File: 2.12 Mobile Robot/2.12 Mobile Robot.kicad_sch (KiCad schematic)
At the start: 27 parts, among them J1 Motor Control R, J2 Motor Control L, J3 GND, J4 Motor Power R, J5 Battery Power, J6 Motor Power L, J7 3.3V, J8 UART, J9 5V, SW1 SW_PWR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

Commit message: Fully routed
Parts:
- R3: renamed from RSE1; Name (none) -> RSE1
- R4: renamed from RCs1; Name (none) -> RCs1
- renumbered R_MTR1 to R1, R_MTR2 to R2, R_MOTOR1 to R5
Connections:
- net L_MOTOR: now reaches F2.2, J6.2
- net R_MOTOR: now reaches F1.2, J4.2
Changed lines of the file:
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@@
   (junction (at 213.36 119.38) (diameter 0) (color 0 0 0 0)
   )
+  (junction (at 206.375 85.09) (diameter 0) (color 0 0 0 0)
+  )
   (junction (at 252.73 119.38) (diameter 0) (color 0 0 0 0)
   )
@@
   (junction (at 201.295 121.285) (diameter 0) (color 0 0 0 0)
   )
+  (junction (at 208.915 64.135) (diameter 0) (color 0 0 0 0)
+  )
   (junction (at 252.73 118.11) (diameter 0) (color 0 0 0 0)
   )
@@
   (junction (at 201.295 116.205) (diameter 0) (color 0 0 0 0)
   )
-  (wire (pts (xy 205.105 64.135) (xy 211.455 64.135))
+  (wire (pts (xy 205.105 64.135) (xy 208.915 64.135))
     (stroke (width 0) (type default))
   )
@@
     (stroke (width 0) (type default))
   )
+  (wire (pts (xy 208.915 69.85) (xy 208.915 64.135))
+    (stroke (width 0) (type default))
+  )
   (wire (pts (xy 233.68 34.925) (xy 244.475 34.925))
     (stroke (width 0) (type default))
@@
     (stroke (width 0) (type default))
   )
+  (wire (pts (xy 206.375 92.075) (xy 206.375 85.09))
+    (stroke (width 0) (type default))
+  )
   (wire (pts (xy 198.755 142.24) (xy 201.295 142.24))
     (stroke (width 0) (type default))
@@
     (stroke (width 0) (type default))
   )
+  (wire (pts (xy 209.55 92.075) (xy 206.375 92.075))
+    (stroke (width 0) (type default))
+  )
   (wire (pts (xy 201.295 113.665) (xy 201.295 116.205))
     (stroke (width 0) (type default))
@@
     (stroke (width 0) (type default))
   )
-  (wire (pts (xy 204.47 85.09) (xy 208.28 85.09))
+  (wire (pts (xy 204.47 85.09) (xy 206.375 85.09))
     (stroke (width 0) (type default))
   )
@@
     (stroke (width 0) (type default))
   )
+  (wire (pts (xy 209.55 69.85) (xy 208.915 69.85))
+    (stroke (width 0) (type default))
+  )
   (wire (pts (xy 73.025 43.18) (xy 83.82 43.18))
     (stroke (width 0) (type default))
   )
+  (wire (pts (xy 206.375 85.09) (xy 208.28 85.09))
+    (stroke (width 0) (type default))
+  )
+  (wire (pts (xy 133.985 71.755) (xy 138.43 71.755))
+    (stroke (width 0) (type default))
+  )
   (wire (pts (xy 204.47 76.2) (xy 204.47 80.01))
     (stroke (width 0) (type default))
@@
   )
   (wire (pts (xy 213.36 119.38) (xy 213.36 121.92))
+    (stroke (width 0) (type default))
+  )
+  (wire (pts (xy 208.915 64.135) (xy 211.455 64.135))
     (stroke (width 0) (type default))
   )
@@
     (effects (font (size 1.27 1.27)) (justify right bottom))
   )
+  (label "L_MOTOR" (at 209.55 69.85 0) (fields_autoplaced)
+    (effects (font (size 1.27 1.27)) (justify left bottom))
+  )
   (label "VBAT_IN" (at 207.645 45.085 0) (fields_autoplaced)
     (effects (font (size 1.27 1.27)) (justify left bottom))
@@
     (effects (font (size 1.27 1.27)) (justify left bottom))
   )
+  (label "R_MOTOR" (at 209.55 92.075 0) (fields_autoplaced)
+    (effects (font (size 1.27 1.27)) (justify left bottom))
+  )
   (label "VBAT_MOTOR" (at 78.74 168.91 0) (fields_autoplaced)
     (effects (font (size 1.27 1.27)) (justify left bottom))
+  )
+  (label "VBAT" (at 133.985 71.755 180) (fields_autoplaced)
+    (effects (font (size 1.27 1.27)) (justify right bottom))
   )
   (label "DIR2_R" (at 73.025 50.8 0) (fields_autoplaced)
@@
   (symbol (lib_id "Device:R_US") (at 153.035 170.18 0) (unit 1)
     (in_bom yes) (on_board yes) (dnp no)
-    (property "Reference" "R_MOTOR1" (at 160.02 172.085 0)
+    (property "Reference" "R5" (at 160.02 172.085 0)
       (effects (font (size 1.27 1.27)))
     )
@@
       (project "2.12 Mobile Robot"
         (path "/7775d959-b998-472b-ab8b-c8b5c0f34c21"
-          (reference "R_MOTOR1") (unit 1)
+          (reference "R5") (unit 1)
         )
       )
@@
   (symbol (lib_id "Device:R_Small_US") (at 27.94 170.815 0) (unit 1)
     (in_bom yes) (on_board yes) (dnp no)
-    (property "Reference" "R_MTR1" (at 30.48 168.91 0)
+    (property "Reference" "R1" (at 30.48 168.91 0)
       (effects (font (size 1.27 1.27)) (justify left))
     )
@@
       (project "2.12 Mobile Robot"
         (path "/7775d959-b998-472b-ab8b-c8b5c0f34c21"
-          (reference "R_MTR1") (unit 1)
+          (reference "R1") (unit 1)
         )
       )
@@
   (symbol (lib_id "Device:R_Small_US") (at 40.005 177.8 0) (mirror y) (unit 1)
     (in_bom yes) (on_board yes) (dnp no)
-    (property "Reference" "RSE1" (at 37.465 177.165 0)
+    (property "Reference" "R3" (at 37.465 177.165 0)
       (effects (font (size 1.27 1.27)) (justify left))
     )
@@
       (effects (font (size 1.27 1.27)) hide)
     )
-    (pin "1")
-    (pin "2")
-    (instances
-      (project "2.12 Mobile Robot"
-        (path "/7775d959-b998-472b-ab8b-c8b5c0f34c21"
-          (reference "RSE1") (unit 1)
+    (property "Name" "RSE1" (at 40.005 177.8 0)
+      (effects (font (size 1.27 1.27)) hide)
+    )
+    (pin "1")
+    (pin "2")
+    (instances
+      (project "2.12 Mobile Robot"
+        (path "/7775d959-b998-472b-ab8b-c8b5c0f34c21"
+          (reference "R3") (unit 1)
         )
       )
@@
   (symbol (lib_id "Device:R_Small_US") (at 75.565 177.8 0) (unit 1)
     (in_bom yes) (on_board yes) (dnp no) (fields_autoplaced)
-    (property "Reference" "RCs1" (at 78.105 177.165 0)
+    (property "Reference" "R4" (at 78.105 177.165 0)
       (effects (font (size 1.27 1.27)) (justify left))
     )
@@
       (effects (font (size 1.27 1.27)) hide)
     )
-    (pin "1")
-    (pin "2")
-    (instances
-      (project "2.12 Mobile Robot"
-        (path "/7775d959-b998-472b-ab8b-c8b5c0f34c21"
-          (reference "RCs1") (unit 1)
+    (property "Name" "RCs1" (at 75.565 177.8 0)
+      (effects (font (size 1.27 1.27)) hide)
+    )
+    (pin "1")
+    (pin "2")
+    (instances
+      (project "2.12 Mobile Robot"
+        (path "/7775d959-b998-472b-ab8b-c8b5c0f34c21"
+          (reference "R4") (unit 1)
         )
       )
@@
   (symbol (lib_id "power:PWR_FLAG") (at 217.805 40.005 0) (unit 1)
     (in_bom yes) (on_board yes) (dnp no)
-    (property "Reference" "#FLG05" (at 217.805 38.1 0)
+    (property "Reference" "#FLG04" (at 217.805 38.1 0)
       (effects (font (size 1.27 1.27)) hide)
     )
@@
       (project "2.12 Mobile Robot"
         (path "/7775d959-b998-472b-ab8b-c8b5c0f34c21"
-          (reference "#FLG05") (unit 1)
+          (reference "#FLG04") (unit 1)
         )
       )
@@
   (symbol (lib_id "Device:R_Small_US") (at 27.94 175.895 0) (mirror y) (unit 1)
     (in_bom yes) (on_board yes) (dnp no)
-    (property "Reference" "R_MTR2" (at 26.67 175.26 0)
+    (property "Reference" "R2" (at 26.67 175.26 0)
       (effects (font (size 1.27 1.27)) (justify left))
     )
@@
       (project "2.12 Mobile Robot"
         (path "/7775d959-b998-472b-ab8b-c8b5c0f34c21"
-          (reference "R_MTR2") (unit 1)
-        )
-      )
+          (reference "R2") (unit 1)
+        )
+      )

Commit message: Made footprints from project libraries
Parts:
- A1: footprint Adafruit:Adafruit_BNO085 -> 2.12_Mobile_Robot:Adafruit_BNO085
- U1: footprint 2.004:DPAK85P972X240-8N -> 2.12_Mobile_Robot:DPAK85P972X240-8N
- U2: footprint footprints:ProS3_TH -> 2.12_Mobile_Robot:ProS3_TH
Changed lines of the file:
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@@
       (effects (font (size 1.27 1.27)))
     )
-    (property "Footprint" "Adafruit:Adafruit_BNO085" (at 38.735 104.14 0)
+    (property "Footprint" "2.12_Mobile_Robot:Adafruit_BNO085" (at 38.735 104.14 0)
       (effects (font (size 1.27 1.27)) hide)
     )
@@
       (effects (font (size 1.27 1.27)))
     )
-    (property "Footprint" "footprints:ProS3_TH" (at 58.547 49.022 0)
+    (property "Footprint" "2.12_Mobile_Robot:ProS3_TH" (at 58.547 49.022 0)
       (effects (font (size 1.27 1.27)) hide)
     )
@@
       (effects (font (size 1.27 1.27)))
     )
-    (property "Footprint" "2.004:DPAK85P972X240-8N" (at 57.785 209.55 0)
+    (property "Footprint" "2.12_Mobile_Robot:DPAK85P972X240-8N" (at 57.785 209.55 0)
       (effects (font (size 1.27 1.27)) (justify bottom) hide)
     )

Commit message: Finesse
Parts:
- A1: footprint 2.12_Mobile_Robot:Adafruit_BNO085 -> Adafruit:Adafruit_BNO085
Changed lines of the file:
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@@
       (effects (font (size 1.27 1.27)))
     )
-    (property "Footprint" "2.12_Mobile_Robot:Adafruit_BNO085" (at 38.735 104.14 0)
+    (property "Footprint" "Adafruit:Adafruit_BNO085" (at 38.735 104.14 0)
       (effects (font (size 1.27 1.27)) hide)
     )

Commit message: Added silkscreen callouts and fixed resistors
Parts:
- R1, R2, R3, R4, R5: footprint Resistor_SMD:R_0201_0603Metric_Pad0.64x0.40mm_HandSolder -> Resistor_SMD:R_0603_1608Metric
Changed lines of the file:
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@@
       (effects (font (size 1.27 1.27)))
     )
-    (property "Footprint" "Resistor_SMD:R_0201_0603Metric_Pad0.64x0.40mm_HandSolder" (at 154.051 170.434 90)
+    (property "Footprint" "Resistor_SMD:R_0603_1608Metric" (at 154.051 170.434 90)
       (effects (font (size 1.27 1.27)) hide)
     )
@@
       (effects (font (size 1.27 1.27)) (justify left))
     )
-    (property "Footprint" "Resistor_SMD:R_0201_0603Metric_Pad0.64x0.40mm_HandSolder" (at 27.94 170.815 0)
+    (property "Footprint" "Resistor_SMD:R_0603_1608Metric" (at 27.94 170.815 0)
       (effects (font (size 1.27 1.27)) hide)
     )
@@
       (effects (font (size 1.27 1.27)) (justify left))
     )
-    (property "Footprint" "Resistor_SMD:R_0201_0603Metric_Pad0.64x0.40mm_HandSolder" (at 40.005 177.8 0)
+    (property "Footprint" "Resistor_SMD:R_0603_1608Metric" (at 40.005 177.8 0)
       (effects (font (size 1.27 1.27)) hide)
     )
@@
       (effects (font (size 1.27 1.27)) (justify left))
     )
-    (property "Footprint" "Resistor_SMD:R_0201_0603Metric_Pad0.64x0.40mm_HandSolder" (at 75.565 177.8 0)
+    (property "Footprint" "Resistor_SMD:R_0603_1608Metric" (at 75.565 177.8 0)
       (effects (font (size 1.27 1.27)) hide)
     )
@@
       (effects (font (size 1.27 1.27)) (justify left))
     )
-    (property "Footprint" "Resistor_SMD:R_0201_0603Metric_Pad0.64x0.40mm_HandSolder" (at 27.94 175.895 0)
-      (effects (font (size 1.27 1.27)) hide)
-    )
+    (property "Footprint" "Resistor_SMD:R_0603_1608Metric" (at 27.94 175.895 0)
+      (effects (font (size 1.27 1.27)) hide)
+    )

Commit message: About to add JLCPCB libraries
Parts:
- removed E1: FL Encoder, Connector_JST:JST_PH_S4B-PH-SM4-TB_1x04-1MP_P2.00mm_Horizontal, symbol Connector:Encoder
- removed E2: BL Encoder, Connector_JST:JST_PH_S4B-PH-SM4-TB_1x04-1MP_P2.00mm_Horizontal, symbol Connector:Encoder
- removed E3: FR Encoder, Connector_JST:JST_PH_S4B-PH-SM4-TB_1x04-1MP_P2.00mm_Horizontal, symbol Connector:Encoder
- removed E4: BR Encoder, Connector_JST:JST_PH_S4B-PH-SM4-TB_1x04-1MP_P2.00mm_Horizontal, symbol Connector:Encoder
- added J10: FL Encoder, Connector_JST:JST_PH_S4B-PH-SM4-TB_1x04-1MP_P2.00mm_Horizontal, symbol Connector_Generic_MountingPin:Conn_01x04_MountingPin
- added J11: BL Encoder, Connector_JST:JST_PH_S4B-PH-SM4-TB_1x04-1MP_P2.00mm_Horizontal, symbol Connector_Generic_MountingPin:Conn_01x04_MountingPin
- added J12: FR Encoder, Connector_JST:JST_PH_S4B-PH-SM4-TB_1x04-1MP_P2.00mm_Horizontal, symbol Connector_Generic_MountingPin:Conn_01x04_MountingPin
- added J13: BR Encoder, Connector_JST:JST_PH_S4B-PH-SM4-TB_1x04-1MP_P2.00mm_Horizontal, symbol Connector_Generic_MountingPin:Conn_01x04_MountingPin
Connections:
- net +3.3V: now also J10.3 (Pin_3), J11.3 (Pin_3), J12.3 (Pin_3), J13.3 (Pin_3)
- net GND: now also J10.4 (Pin_4), J10.MP (MountPin), J11.4 (Pin_4), J11.MP (MountPin), J12.4 (Pin_4), J12.MP (MountPin), J13.4 (Pin_4), J13.MP (MountPin)
- net HALL_BL_A: now also J11.1 (Pin_1)
- net HALL_BL_B: now also J11.2 (Pin_2)
- net HALL_BR_A: now also J13.1 (Pin_1)
- net HALL_BR_B: now also J13.2 (Pin_2)
- net HALL_FL_A: now also J10.1 (Pin_1)
- net HALL_FL_B: now also J10.2 (Pin_2)
- net HALL_FR_A: now also J12.1 (Pin_1)
- net HALL_FR_B: now also J12.2 (Pin_2)

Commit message: Tentatively ready for production
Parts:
- A1, U2: now left out of the parts list
- D1: footprint LED_SMD:LED_0603_1608Metric -> footprint:LED0603; symbol Device:LED -> jlcpcb-diodes:0603,Red; LCSC (none) -> C2286; MPN C434423 -> (none)
- J4, J6: LCSC (none) -> C2913282
- J5: footprint Connector_AMASS:AMASS_XT60PW-M_1x02_P7.20mm_Horizontal -> Connector_AMASS:AMASS_XT30PW-M_1x02_P2.50mm_Horizontal; LCSC (none) -> C2913282
- J9, SW1: now in the parts list
- R1, R2: footprint Resistor_SMD:R_0603_1608Metric -> footprint:0603_1608Metric; symbol Device:R_Small_US -> jlcpcb-basic-resistor:0603,15k; LCSC (none) -> C22809; MFG (none) -> UNI-ROYAL(Uniroyal Elec); MFGPN (none) -> 0603WAF1502T5E; MPN C114661 -> (none)
- R3: footprint Resistor_SMD:R_0603_1608Metric -> footprint:0603_1608Metric; symbol Device:R_Small_US -> jlcpcb-basic-resistor:0603,15k; LCSC (none) -> C22809; MFG (none) -> UNI-ROYAL(Uniroyal Elec); MFGPN (none) -> 0603WAF1502T5E; MPN C114661 -> (none); Name RSE1 -> (none)
- R4: footprint Resistor_SMD:R_0603_1608Metric -> footprint:0603_1608Metric; symbol Device:R_Small_US -> jlcpcb-basic-resistor:0603,15k; LCSC (none) -> C22809; MFG (none) -> UNI-ROYAL(Uniroyal Elec); MFGPN (none) -> 0603WAF1502T5E; MPN C114661 -> (none); Name RCs1 -> (none)
- R5: footprint Resistor_SMD:R_0603_1608Metric -> footprint:0603_1608Metric; symbol Device:R_US -> jlcpcb-basic-resistor:0603,1k; LCSC (none) -> C21190; MFG (none) -> UNI-ROYAL(Uniroyal Elec); MFGPN (none) -> 0603WAF1001T5E
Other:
- sheet Buck ports: added none; removed VBAT_MCU

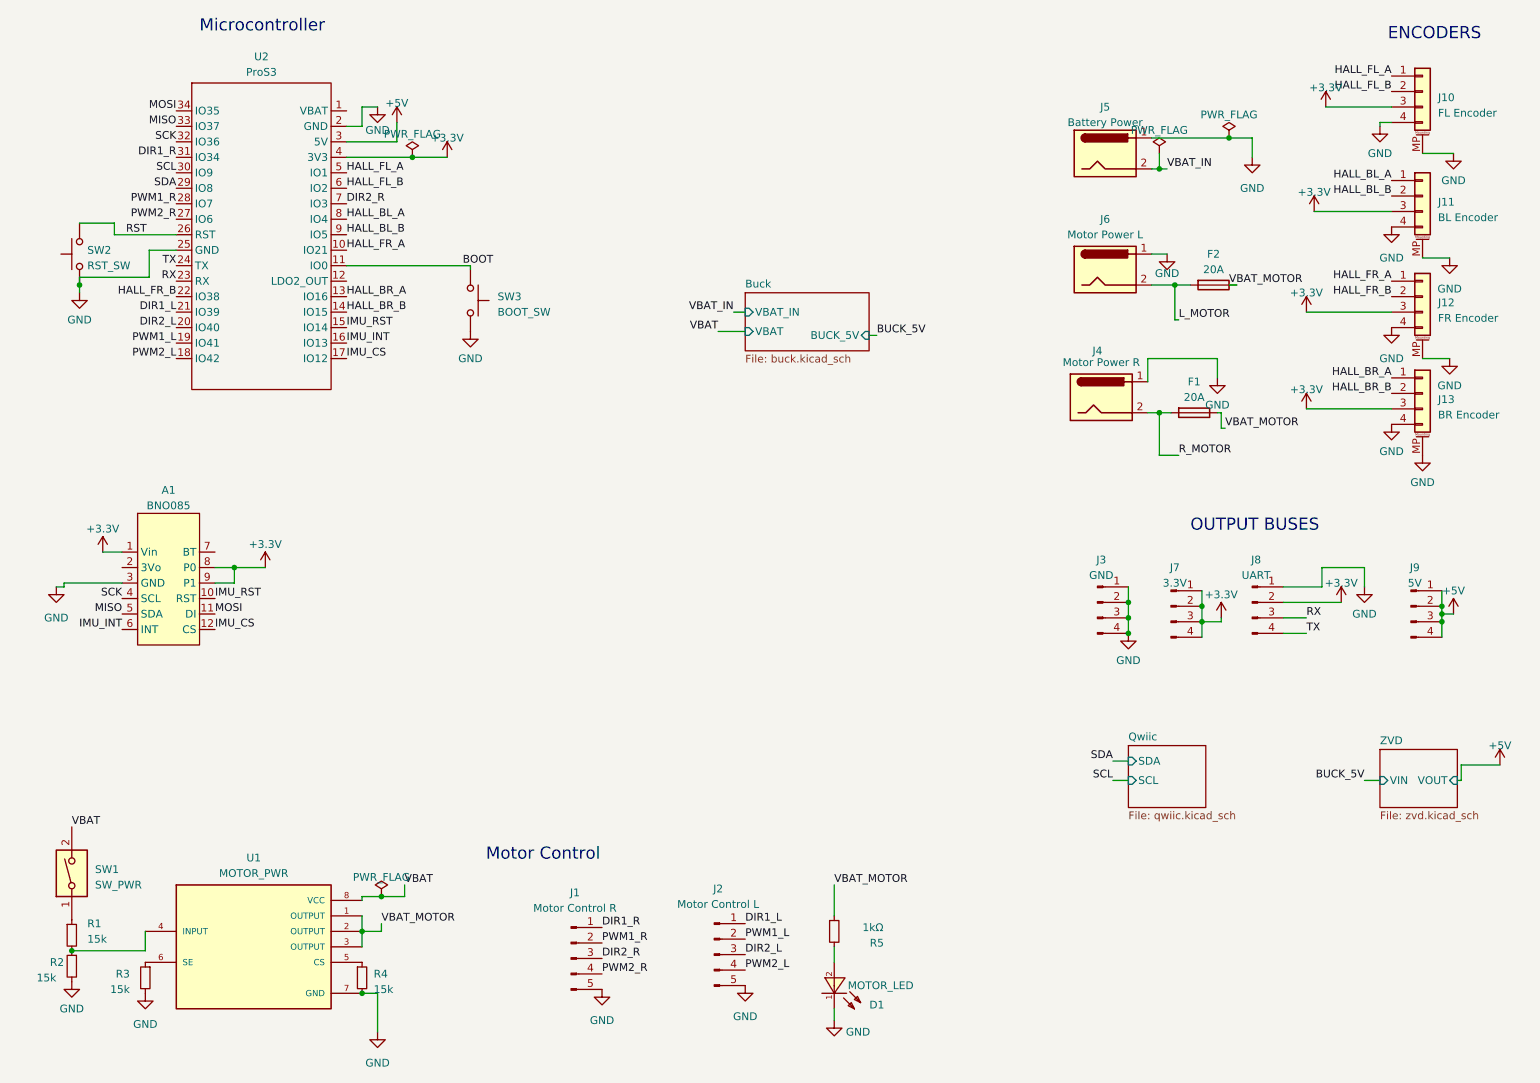
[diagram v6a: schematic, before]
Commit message: Updated silkscreen to be generic
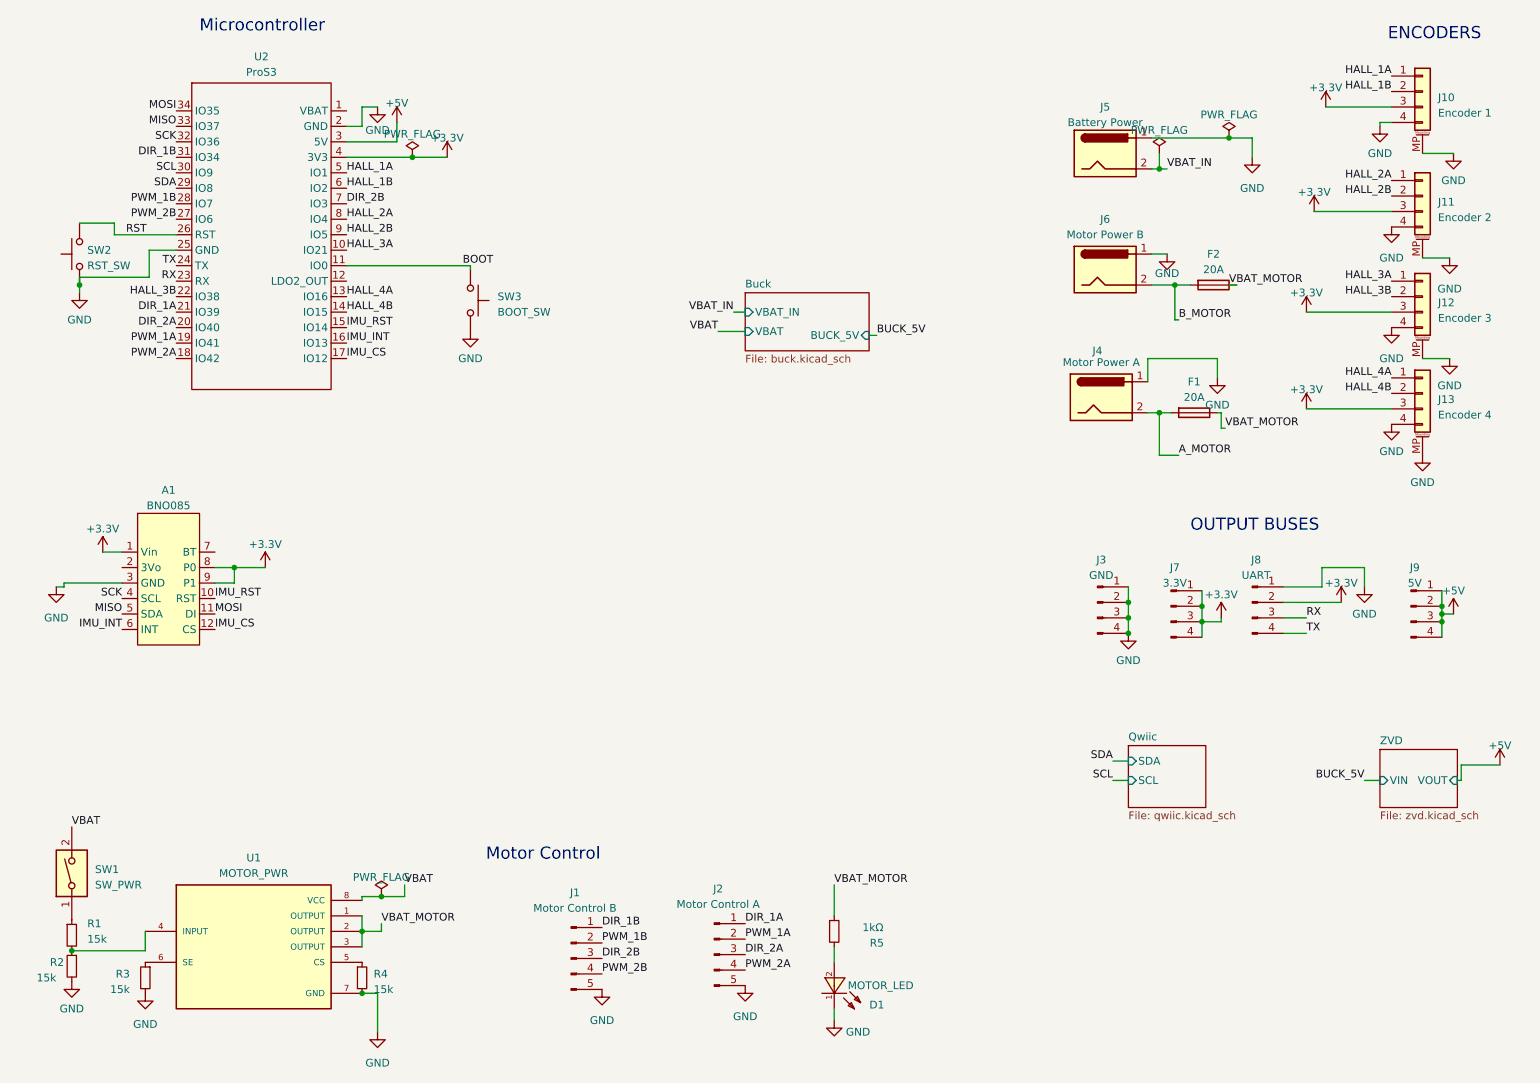
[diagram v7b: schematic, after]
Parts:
- J1: value Motor Control R -> Motor Control B
- J10: value FL Encoder -> Encoder 1
- J11: value BL Encoder -> Encoder 2
- J12: value FR Encoder -> Encoder 3
- J13: value BR Encoder -> Encoder 4
- J2: value Motor Control L -> Motor Control A
- J4: value Motor Power R -> Motor Power A
- J6: value Motor Power L -> Motor Power B
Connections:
- net DIR1_L renamed DIR_1A
- net DIR1_R renamed DIR_1B
- net DIR2_L renamed DIR_2A
- net DIR2_R renamed DIR_2B
- net HALL_BL_A renamed HALL_2A
- net HALL_BL_B renamed HALL_2B
- net HALL_BR_A renamed HALL_4A
- net HALL_BR_B renamed HALL_4B
- net HALL_FL_A renamed HALL_1A
- net HALL_FL_B renamed HALL_1B
- net HALL_FR_A renamed HALL_3A
- net HALL_FR_B renamed HALL_3B
- net L_MOTOR renamed B_MOTOR
- net PWM1_L renamed PWM_1A
- net PWM1_R renamed PWM_1B
- net PWM2_L renamed PWM_2A
- net PWM2_R renamed PWM_2B
- net R_MOTOR renamed A_MOTOR
